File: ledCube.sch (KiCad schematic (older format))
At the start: 13 parts, among them P1 CONN_01X03, P2 CONN_01X02, P3 CONN_01X02, P4 CONN_01X02, P5 CONN_01X02, U1 AL8805W5

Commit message: Generate BOM & Gerber
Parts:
- R1, R2: Part # (none) -> 311-0.5LWCT-ND; Vender (none) -> DigiKey
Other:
- note added: "Lower Board"
- note added: "Upper Board"
- moved on the sheet: C1, C2, D1, D2, L1, P1, P2, P3, P4, P5, R1, R2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

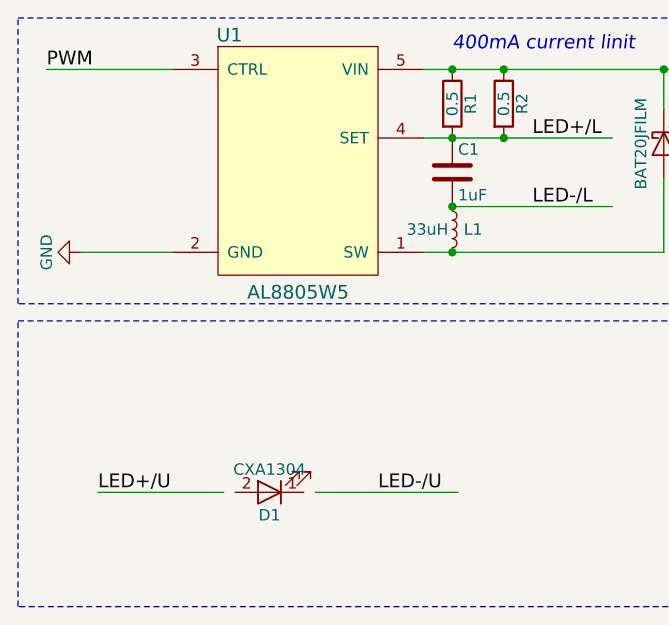
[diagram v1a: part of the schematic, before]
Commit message: pull down PWM line
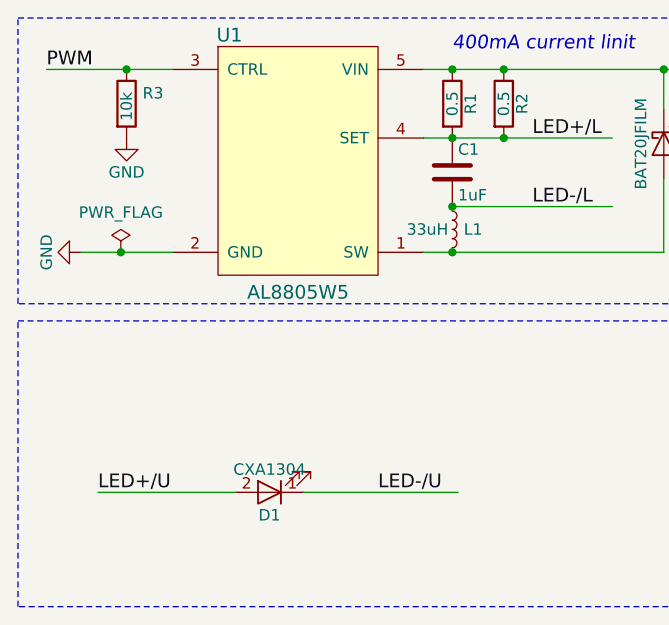
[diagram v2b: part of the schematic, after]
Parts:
- added R3: 10k, Capacitors_SMD:C_0603, symbol R
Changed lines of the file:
@@
 EESchema Schematic File Version 2
+LIBS:ledCube-rescue
 LIBS:power
 LIBS:device
@@
 LIBS:custom
 LIBS:ledCube-cache
-EELAYER 25 0
+EELAYER 26 0
 EELAYER END
 $Descr A4 11693 8268
@@
 $EndComp
 Wire Wire Line
-	3875 4625 3325 4625
-Wire Wire Line
-	4275 4625 4900 4625
+	3325 4625 3925 4625
+Wire Wire Line
+	4225 4625 4900 4625
 Text Label 3325 4625 0    60   ~ 0
 LED+/U
@@
 Text Notes 8050 4000 0    60   Italic 0
 Upper Board
+$Comp
+L R R3
+U 1 1 586A07C4
+P 3450 2925
+F 0 "R3" H 3520 2971 50  0000 L CNN
+F 1 "10k" V 3450 2850 50  0000 L CNN
+F 2 "Capacitors_SMD:C_0603" H 3520 2834 50  0001 L CNN
+F 3 "" H 3450 2925 50  0000 C CNN
+	1    3450 2925
+	1    0    0    -1
+$EndComp
+$Comp
+L GND #PWR04
+U 1 1 586A0877
+P 3450 3075
+F 0 "#PWR04" H 3450 2825 50  0001 C CNN
+F 1 "GND" H 3450 2925 50  0000 C CNN
+F 2 "" H 3450 3075 50  0000 C CNN
+F 3 "" H 3450 3075 50  0000 C CNN
+	1    3450 3075
+	1    0    0    -1
+$EndComp
+Connection ~ 3450 2775
+$Comp
+L PWR_FLAG #FLG?
+U 1 1 586A0E3F
+P 3425 3575
+F 0 "#FLG?" H 3425 3650 50  0001 C CNN
+F 1 "PWR_FLAG" H 3425 3749 50  0000 C CNN
+F 2 "" H 3425 3575 50  0000 C CNN
+F 3 "" H 3425 3575 50  0000 C CNN
+	1    3425 3575
+	1    0    0    -1
+$EndComp
+Connection ~ 3425 3575
 $EndSCHEMATC
